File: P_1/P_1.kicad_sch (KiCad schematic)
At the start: 7 parts, among them Q1 2N2219, U1 INA225

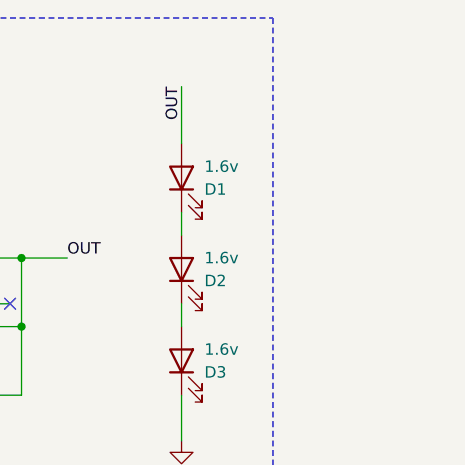
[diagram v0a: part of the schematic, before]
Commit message: Cambio con SSH
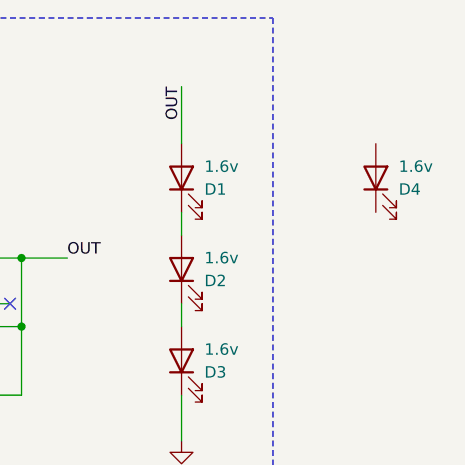
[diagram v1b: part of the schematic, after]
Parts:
- added D4: 1.6v, Transistor_Power:GaN_Systems_GaNPX-3_5x6.6mm_Drain3.76x0.6mm, symbol Device:LED

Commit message: Ahora
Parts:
- added D5: 1.6v, Transistor_Power:GaN_Systems_GaNPX-3_5x6.6mm_Drain3.76x0.6mm, symbol Device:LED
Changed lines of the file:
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@@
+		)
+	)
+	(symbol
+		(lib_id "Device:LED")
+		(at 184.15 53.34 90)
+		(unit 1)
+		(exclude_from_sim no)
+		(in_bom yes)
+		(on_board yes)
+		(dnp no)
+		(property "Reference" "D5"
+			(at 186.69 54.61 90)
+			(effects
+				(font
+					(size 1.27 1.27)
+				)
+				(justify right)
+			)
+		)
+		(property "Value" "1.6v"
+			(at 186.69 52.07 90)
+			(effects
+				(font
+					(size 1.27 1.27)
+				)
+				(justify right)
+			)
+		)
+		(property "Footprint" "Transistor_Power:GaN_Systems_GaNPX-3_5x6.6mm_Drain3.76x0.6mm"
+			(at 184.15 53.34 0)
+			(effects
+				(font
+					(size 1.27 1.27)
+				)
+				(hide yes)
+			)
+		)
+		(property "Datasheet" "~"
+			(at 184.15 53.34 0)
+			(effects
+				(font
+					(size 1.27 1.27)
+				)
+				(hide yes)
+			)
+		)
+		(property "Description" ""
+			(at 184.15 53.34 0)
+			(effects
+				(font
+					(size 1.27 1.27)
+				)
+				(hide yes)
+			)
+		)
+		(pin "2"
+		)
+		(pin "1"
+		)
+		(instances
+			(project "P_1"
+				(path "/87f75057-1bd3-4400-84e5-4864f72e22bf"
+					(reference "D5")
+					(unit 1)
+				)
+			)
 		)
 	)
